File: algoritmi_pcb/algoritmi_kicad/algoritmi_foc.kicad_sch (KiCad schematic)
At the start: 10 parts, among them U1 TMC6300-LA-T

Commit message: Updates to the schematics
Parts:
- removed C1, C2, C3: 100nF, CAPC1608X95N, symbol SamacSys_Parts:C0603C104K8RAC
- added C1, C2, C3, C4: 100nF 50V, CAPC1608X90N, symbol SamacSys_Parts:CL10B104KB8NNWC
- added C5: 10uF 25V, CAPC2012X145N, symbol SamacSys_Parts:CL21A106KAYNNNE
- added R10, R5, R6, R7, R8, R9: 100K, RESC1608X55N, symbol SamacSys_Parts:CMP0603-FX-1003ELF
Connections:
- net GND: now also C1., C2., C3., C5., R10., R5., R6., R7., R8., R9.
- net at U1.11 (VIO/NSTDBY): now also D1. (K), C3.; no longer D1.2 (A)
- net VL: now reaches U1.10 (VL)
- net VL: now also R10.
- net at U1.12 (DIAG): now also D2. (K); no longer D2.2 (A)
- net at U1.13 (1.8VOUT): now also C2.
- net VCP: now reaches U1.2 (VCP)
- net VCP: now also C4.
- net UH: now reaches U1.3 (UH)
- net UH: now also R5.
- net VH: now reaches U1.4 (VH)
- net VH: now also R6.
- net WH: now reaches U1.5 (WH)
- net WH: now also R7.
- net UL: now reaches U1.6 (UL)
- net UL: now also R8.
- net WL: now reaches U1.7 (WL)
- net WL: now also R9.
- net VS renamed +5V
- net +5V: now also C1., C4., C5.
- new net: D1. (K), R1.
- new net: D2. (K), R2.
- no-connect marks 1 -> 0

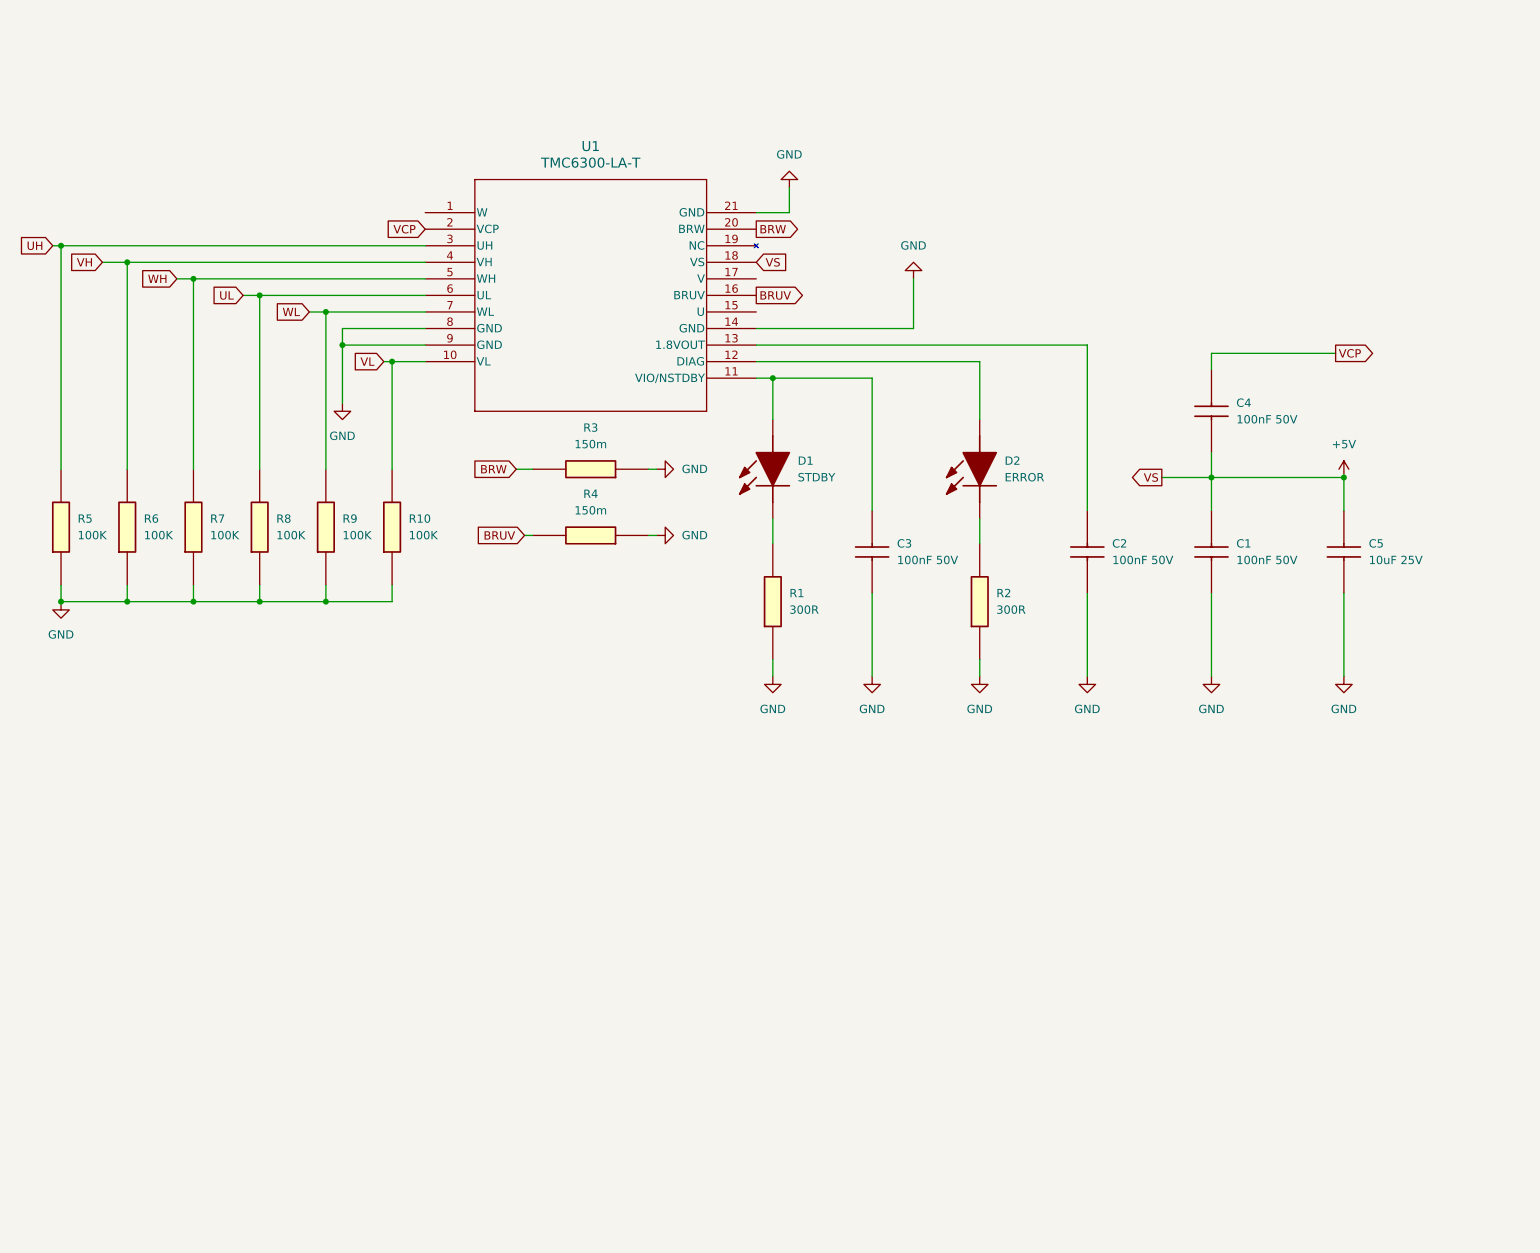
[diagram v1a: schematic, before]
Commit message: Schematics: Added Power and Encoder
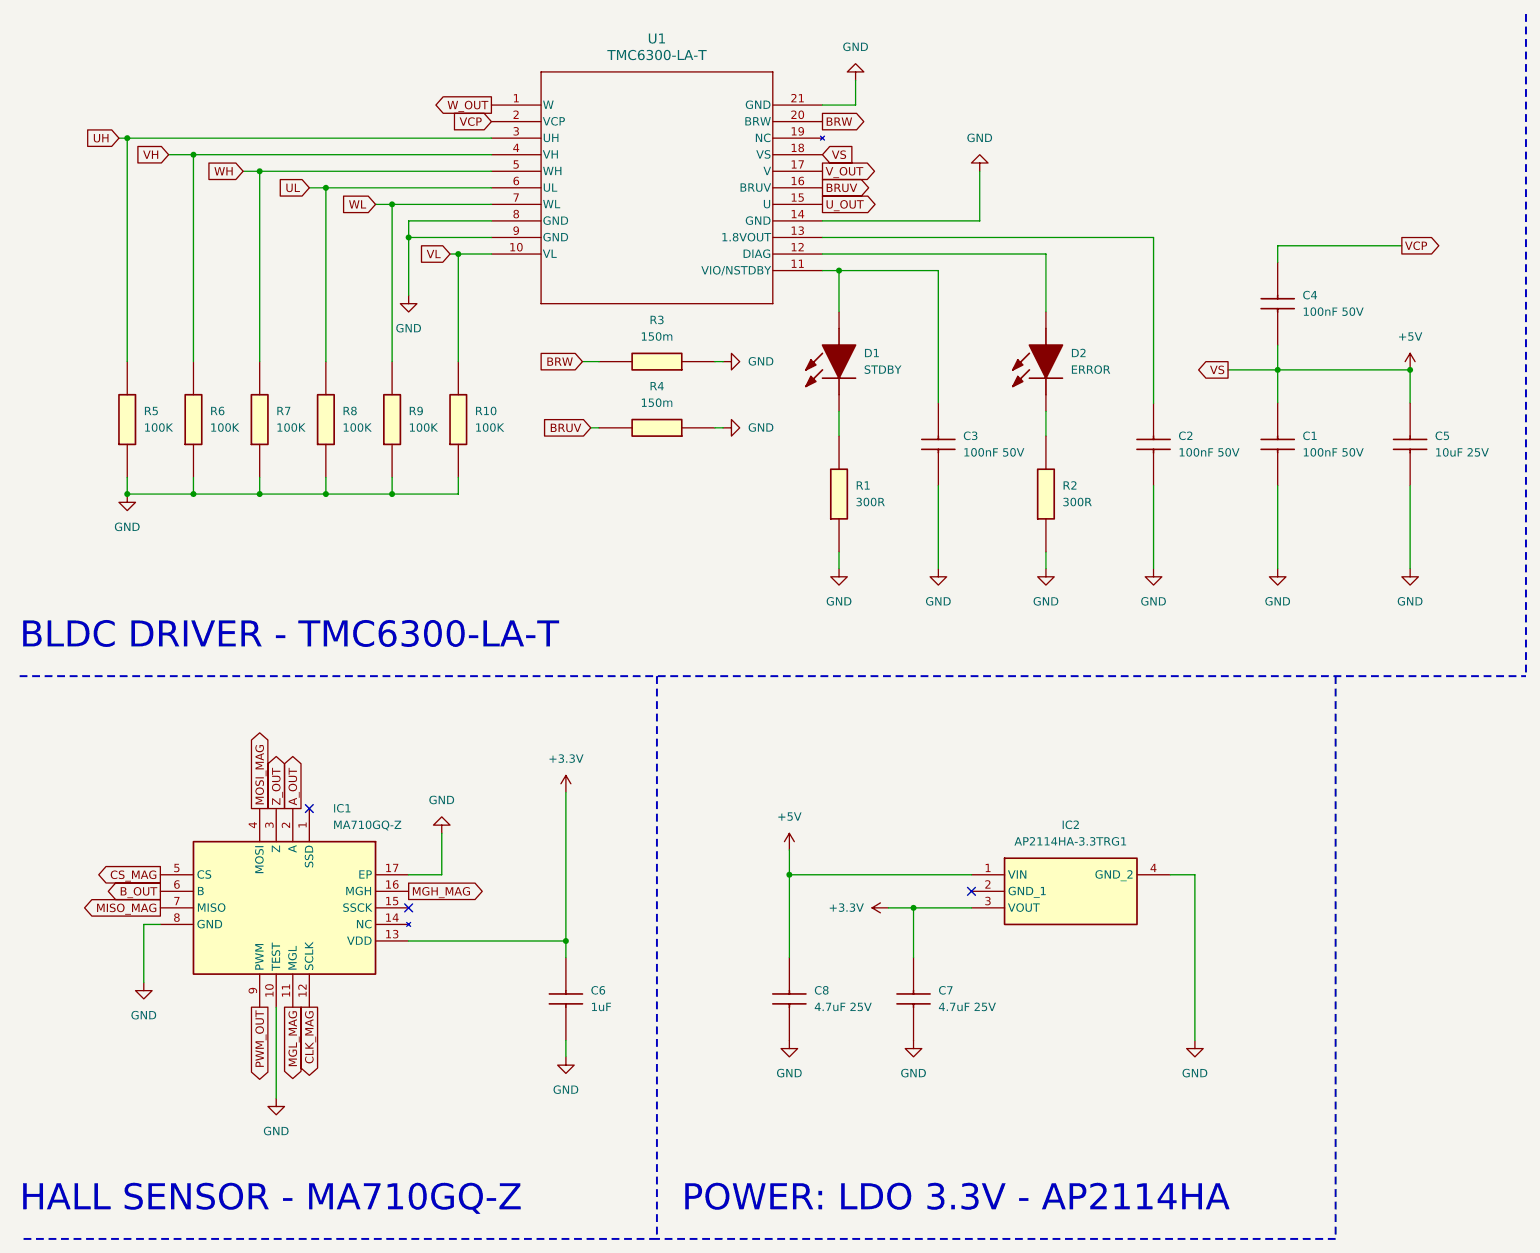
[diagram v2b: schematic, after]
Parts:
- added C6: 1uF, CAPC1608X90N, symbol SamacSys_Parts:CL10A105KA8NNNC
- added C7, C8: 4.7uF 25V, CAPC2012X140N, symbol SamacSys_Parts:GCM21BC71E475KE36K
- added IC1: MA710GQ-Z, QFN50P300X300X100-17N-D, symbol SamacSys_Parts:MA710GQ-Z
- added IC2: AP2114HA-3.3TRG1, SOT230P700X180-4N, symbol SamacSys_Parts:AP2114HA-3.3TRG1
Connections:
- net +5V: now also C8., IC2.1 (VIN)
- net GND: now also C6., C7., C8., IC1.10 (TEST), IC1.17 (EP), IC1.8 (GND), IC2.4 (GND_2)
- net at D1. (K): now also C3., U1.11 (VIO/NSTDBY); no longer R1.
- net at D2. (K): now also U1.12 (DIAG); no longer R2.
- net W_OUT: now reaches U1.1 (W)
- net U_OUT: now reaches U1.15 (U)
- net V_OUT: now reaches U1.17 (V)
- new net: D1. (K), R1.
- new net: D2. (K), R2.
- new net +3.3V: C6., C7., IC1.13 (VDD), IC2.3 (VOUT)
- new net A_OUT: IC1.2 (A)
- new net B_OUT: IC1.6 (B)
- new net CLK_MAG: IC1.12 (SCLK)
- new net CS_MAG: IC1.5 (CS)
- new net MGH_MAG: IC1.16 (MGH)
- new net MGL_MAG: IC1.11 (MGL)
- new net MISO_MAG: IC1.7 (MISO)
- new net MOSI_MAG: IC1.4 (MOSI)
- new net PWM_OUT: IC1.9 (PWM)
- new net Z_OUT: IC1.3 (Z)
- no-connect marks 0 -> 3
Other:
- note added: "BLDC DRIVER - TMC6300-LA-T"
- note added: "HALL SENSOR - MA710GQ-Z"
- note added: "POWER: LDO 3.3V - AP2114HA"
- company: (none) -> University of Minho - Centro Algoritmi
- title: (none) -> ALGORITMI_SMARTKNOB_FOC
- moved on the sheet: C1, C2, C3, C4, C5, D1, D2, R1, R10, R2, R3, R4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

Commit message: Final Schematics and started PCB design
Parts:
- added C9: 10uF 25V, CAPC2012X145N, symbol SamacSys_Parts:CL21A106KAYNNNE
- added J1: ~, solder_pads:solder_pads_2mm_8, symbol solder_pad:solder_pad_2mm_8
- added MSW1: ~, solder_pads:solder_pads_4mm_3, symbol solder_pad:solder_pad_4mm_3
- added R11: 300R, ERJUP3, symbol SamacSys_Parts:ERJ-UP3F3000V
- U1: footprint 21-100586_K2033+1C_ADI -> SamacSys_Parts:QFN40P300X300X90-21N
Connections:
- net +3.3V: now also C6.2, C7.2, C9.2, J1.1; no longer C6., C7.
- net +5V: now also C1.2, C4.1, C5.2, C8.2, R11.2; no longer C1., C4., C5., C8.
- net BRUV: now also R4.1; no longer R4.
- net BRW: now also R3.1; no longer R3.
- net GND: now also C1.1, C2.1, C3.1, C5.1, C6.1, C7.1, C8.1, R1.1, R10.1, R2.1, R3.2, R4.2, R5.1, R6.1, R7.1, R8.1, R9.1, C9.1, J1.2, MSW1.1 (COM); no longer C1., C2., C3., C5., C6., C7., C8., R1., R10., R2., R3., R4., R5., R6., R7., R8., R9.
- net UH: now also R5.2; no longer R5.
- net UL: now also R8.2; no longer R8.
- net VCP: now also C4.2; no longer C4.
- net VH: now also R6.2; no longer R6.
- net VL: now also R10.2; no longer R10.
- net WH: now also R7.2; no longer R7.
- net WL: now also R9.2; no longer R9.
- net at U1.12 (DIAG): now also D2.2 (A); no longer D2. (K)
- net at U1.13 (1.8VOUT): now also C2.2; no longer C2.
- new net: D1.1 (K), R1.2
- new net: C3.2, D1.2 (A), U1.11 (VIO/NSTDBY)
- new net: D2.1 (K), R2.2
- new net LCD_BL: J1.8
- new net LCD_CLOCK: J1.4
- new net LCD_CS: J1.5
- new net LCD_DATA_IN: J1.3
- new net LCD_DC: J1.6
- new net LCD_RESET: J1.7
- new net SW_OUT: MSW1.4 (NO), R11.1
- no-connect marks 3 -> 4
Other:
- note added: "MICROSWITCH CIRCUIT"
- note added: "ROUND LCD CONNECTOR 1.28" GC9A01 DRIVER"

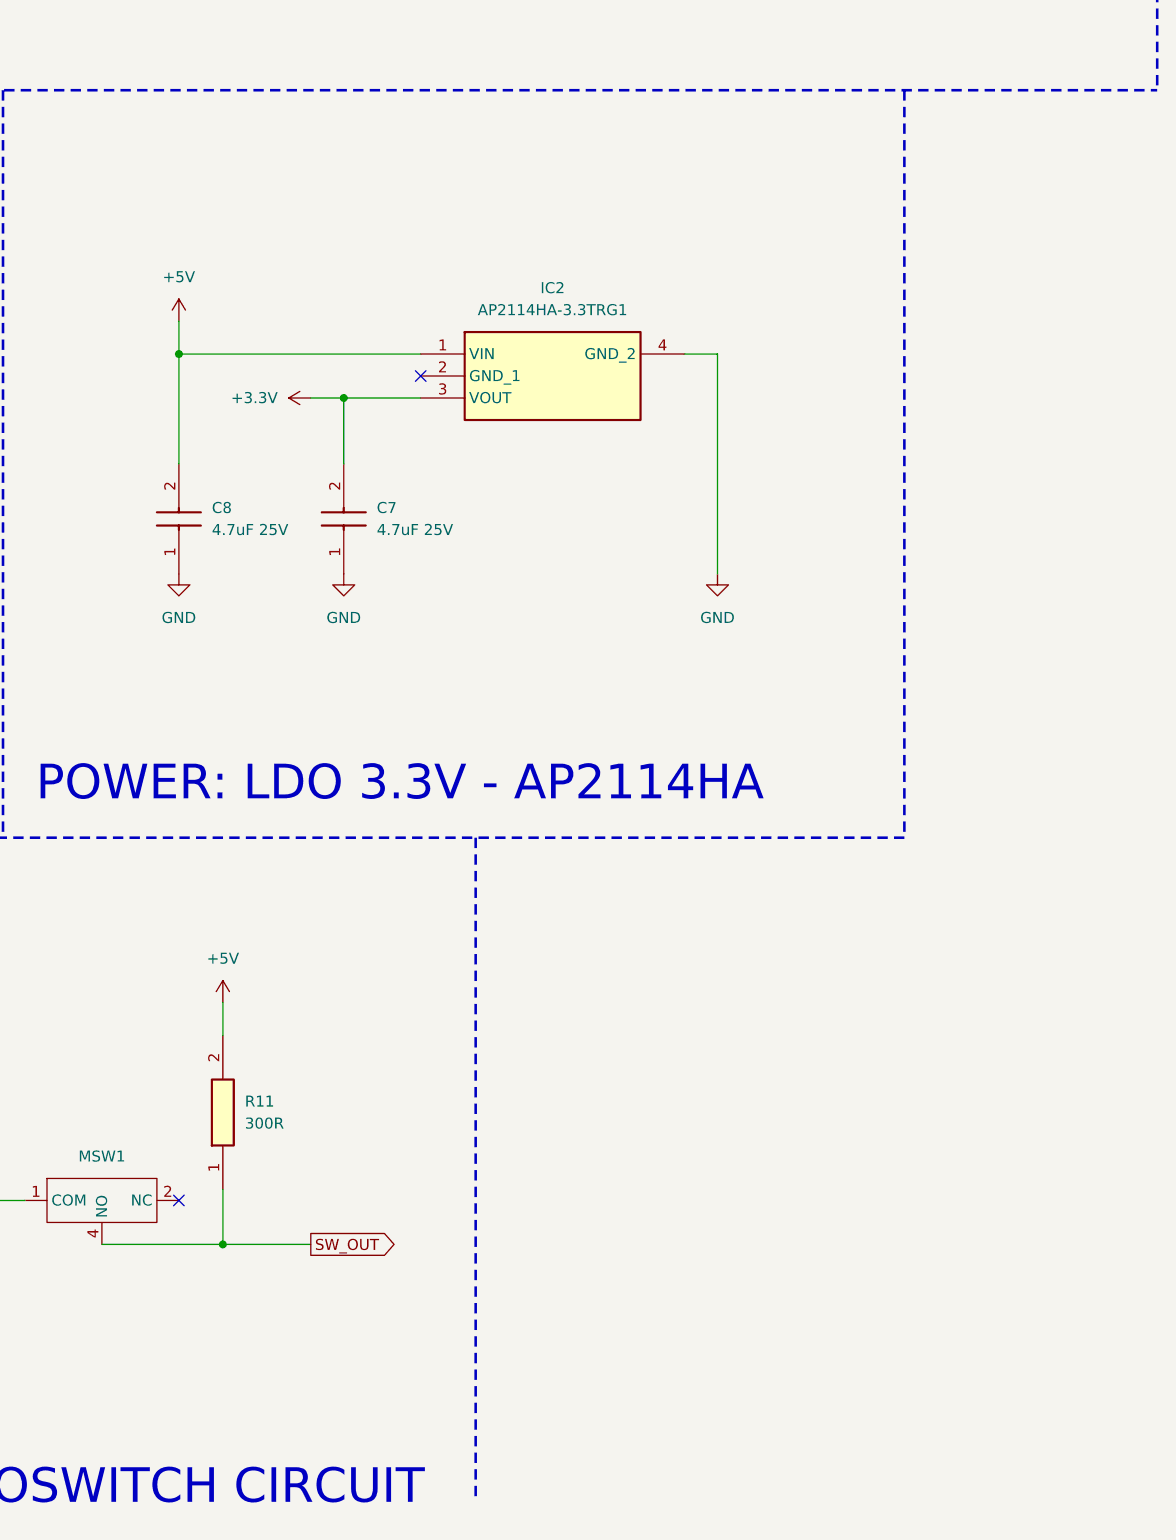
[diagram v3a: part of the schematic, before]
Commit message: Update PCB and Design
Design: added the connector for the motor.

PCB: added some constraints and essentially connected all the components to the TMC6300-LA-T.
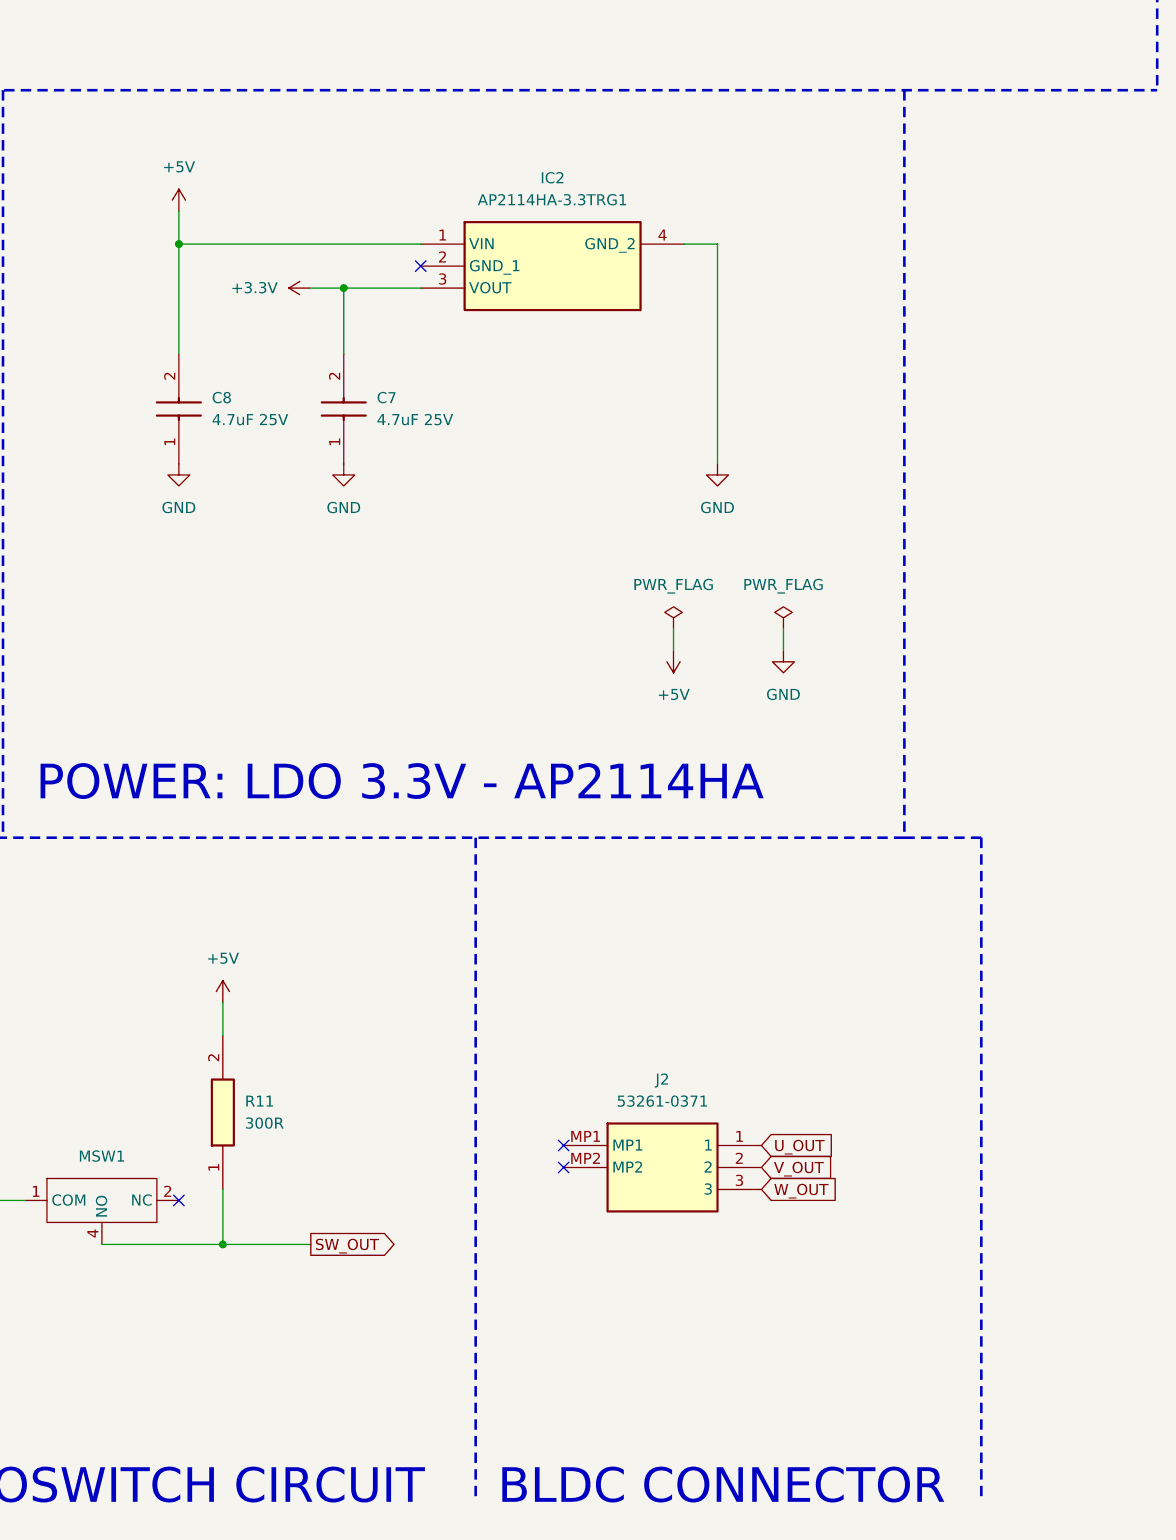
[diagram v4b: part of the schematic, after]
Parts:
- added J2: 53261-0371, 532610371, symbol SamacSys_Parts:53261-0371
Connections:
- net U_OUT: now also J2.1
- net V_OUT: now also J2.2
- net W_OUT: now also J2.3
- no-connect marks 4 -> 6
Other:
- note added: "BLDC CONNECTOR"
- moved on the sheet: C7, C8, IC2

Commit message: More PCB and Schematics Design
Also added components to the library.
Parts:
- added J3: SMM-115-02-S-D-LC-K-TR, SMM11502SDLCKTR, symbol SamacSys_Parts:SMM-115-02-S-D-LC-K-TR
- added MSW2, MSW3, MSW4: ~, solder_pads:solder_pads_4mm_3, symbol solder_pad:solder_pad_4mm_3
- added R12, R13, R14: 300R, ERJUP3, symbol SamacSys_Parts:ERJ-UP3F3000V
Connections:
- net +5V: now also J3.28, J3.30, R12.2, R13.2, R14.2
- net A_OUT: now also J3.12
- net B_OUT: now also J3.10
- net CLK_MAG: now also J3.20
- net CS_MAG: now also J3.22
- net GND: now also J3.24, J3.26, MSW2.1 (COM), MSW3.1 (COM), MSW4.1 (COM)
- net LCD_BL: now also J3.1
- net LCD_CLOCK: now also J3.9
- net LCD_CS: now also J3.7
- net LCD_DATA_IN: now also J3.11
- net LCD_DC: now also J3.5
- net LCD_RESET: now also J3.3
- net MISO_MAG: now also J3.18
- net MOSI_MAG: now also J3.16
- net PWM_OUT: now also J3.6
- net UH: now also J3.29
- net UL: now also J3.23
- net VH: now also J3.27
- net VL: now also J3.21
- net WH: now also J3.25
- net WL: now also J3.19
- net Z_OUT: now also J3.8
- net SW_OUT renamed SW1_OUT
- net SW1_OUT: now also J3.17
- new net SW2_OUT: J3.15, MSW2.4 (NO), R12.1
- new net SW3_OUT: J3.4, MSW3.4 (NO), R13.1
- new net SW4_OUT: J3.2, MSW4.4 (NO), R14.1
- no-connect marks 6 -> 9
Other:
- note added: "GPIO INTERFACE"
- moved on the sheet: J2, MSW1, R11
